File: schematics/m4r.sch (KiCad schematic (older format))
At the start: 93 parts

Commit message: Rename schematics folder and delete old board template
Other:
- note removed: "GLOBAL INTERCONNECTS"
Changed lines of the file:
@@
 Text Label 5550 9400 0    60   ~ 0
 JTCK
-Text Notes 650  750  0    98   ~ 20
-GLOBAL INTERCONNECTS
 $Comp
 L cusf-kicad:SWD_TC P?
@@
 JTDR
 Wire Notes Line
-	650  2950 3850 2950
-Wire Notes Line
-	3850 2950 3850 800
-Wire Notes Line
-	3850 800  650  800
-Wire Notes Line
-	650  800  650  2950
-Wire Notes Line
 	4400 8450 650  8450

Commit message: Chain JTAG connections
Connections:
- net JTDR renamed JTDO
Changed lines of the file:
@@
 JTDI
 Text Label 2950 4200 0    60   ~ 0
-JTDR
+JTDO
 Text Label 5550 9300 0    60   ~ 0
 JTMS
@@
 CAN_RXD
 Text Label 5550 9600 0    60   ~ 0
-JTDR
+JTDO
 Wire Notes Line
 	4400 8450 650  8450
@@
 JTDI
 Text HLabel 5400 9600 0    50   Input ~ 0
-JTDR
+JTDO
 Text HLabel 5400 9700 0    50   Input ~ 0
 3V3

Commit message: Master layout reorganisation and cleanup
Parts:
- removed C? (x2): 100n, agg:0402, symbol cusf-kicad:C
- removed C? (x2): 2µ2, agg:0402, symbol cusf-kicad:C
- removed D?: GRN, agg:0603-LED, symbol cusf-kicad:LED
- removed IC?: STM32F405RxTx, agg:LQFP-64, symbol cusf-kicad:STM32F405RxTx
- removed R?: 100, agg:0402, symbol cusf-kicad:R
- added C33, C38: 100n, agg:0402, symbol cusf-kicad:C
- added C42, C43: 2µ2, agg:0402, symbol cusf-kicad:C
- added D13: GRN, agg:0603-LED, symbol cusf-kicad:LED
- added IC9: STM32F405RxTx, agg:LQFP-64, symbol cusf-kicad:STM32F405RxTx
- added R16: 100, agg:0402, symbol cusf-kicad:R
- gave numbers to parts that had none: 86
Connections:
- net 3v3: now also C38.2, IC9.1 (VBAT), IC9.13 (VDDA), IC9.19 (VDD), IC9.32 (VDD), IC9.48 (VDD), IC9.64 (VDD)
- net 5V_CAN: now also C33.1
- net ANT_~EN: now also IC9.4 (PC15)
- net ANT_~FLAG: now also IC9.3 (PC14)
- net CAN_RXD: now also IC9.61 (PB8)
- net CAN_TXD: now also IC9.62 (PB9)
- net GND: now also C33.2, C38.1, C42.2, C43.2, D13.1, IC9.12 (VSSA), IC9.18 (VSS), IC9.60 (BOOT0), IC9.63 (VSS)
- net GPS_PPS: now also IC9.21 (PA5)
- net GPS_RESET_N: now also IC9.16 (PA2)
- net GPS_RX: now also IC9.14 (PA0)
- net GPS_TX: now also IC9.15 (PA1)
- net JTCK: now also IC9.49 (PA14)
- net JTDI: now also IC9.50 (PA15)
- net JTDO: now also IC9.55 (PB3)
- net JTMS: now also IC9.46 (PA13)
- net LED_GRN: now also IC9.11 (PC3), R16.1
- net LED_RED: now also IC9.9 (PC1)
- net LED_YLW: now also IC9.10 (PC2)
- net MCU_CLK: now also IC9.5 (PH0)
- net PLL_SCL: now also IC9.29 (PB10)
- net PLL_SDA: now also IC9.30 (PB11)
- net RADIO_GATE: now also IC9.41 (PA8)
- net RADIO_GPIO1: now also IC9.45 (PA12)
- net RADIO_SCLK: now also IC9.34 (PB13)
- net RADIO_SDI: now also IC9.36 (PB15)
- net RADIO_SDN: now also IC9.37 (PC6)
- net RADIO_SDO: now also IC9.35 (PB14)
- net RADIO_nIRQ: now also IC9.44 (PA11)
- net RADIO_nSEL: now also IC9.17 (PA3)
- net ~RST: now also IC9.7 (NRST)
- new net: D13.2, R16.2
- new net: C43.1, IC9.31 (VCAP_1)
- new net: C42.1, IC9.47 (VCAP_2)

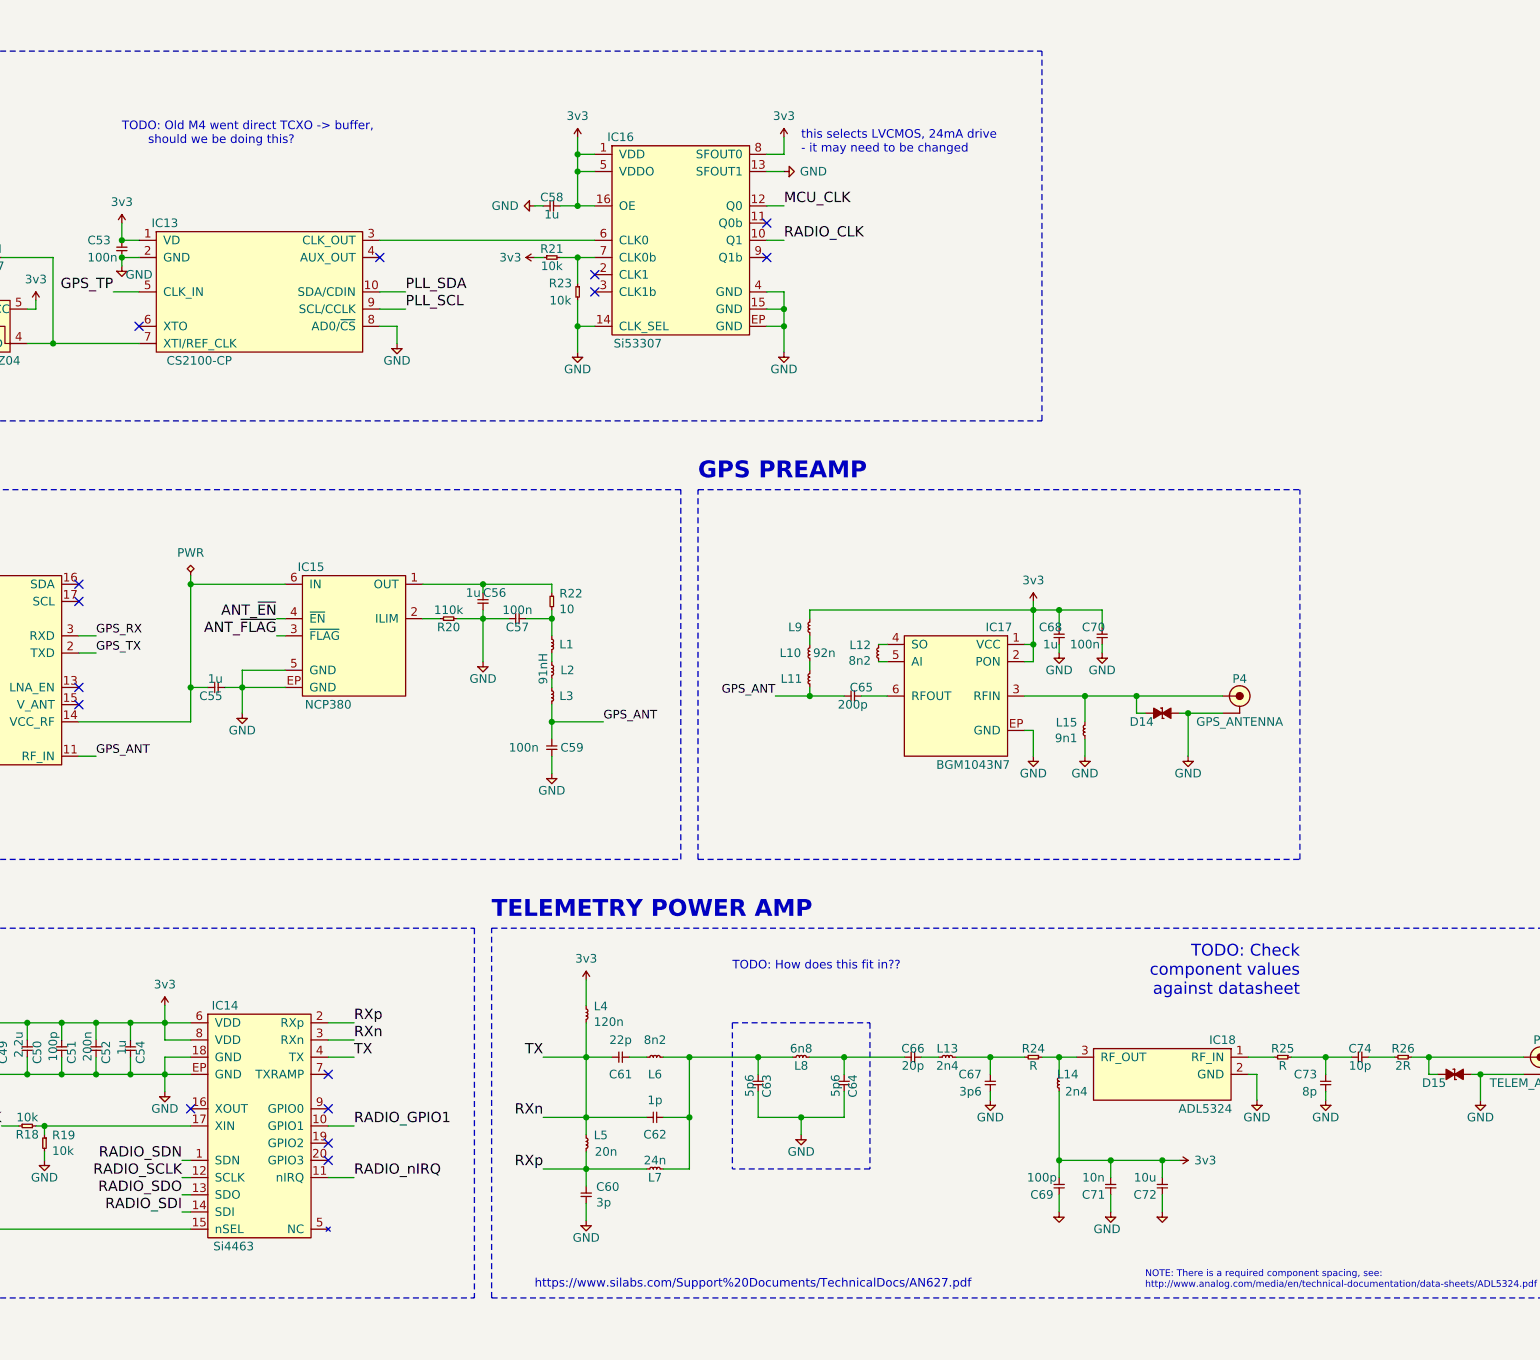
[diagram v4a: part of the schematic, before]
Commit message: Fix telemetry power amp
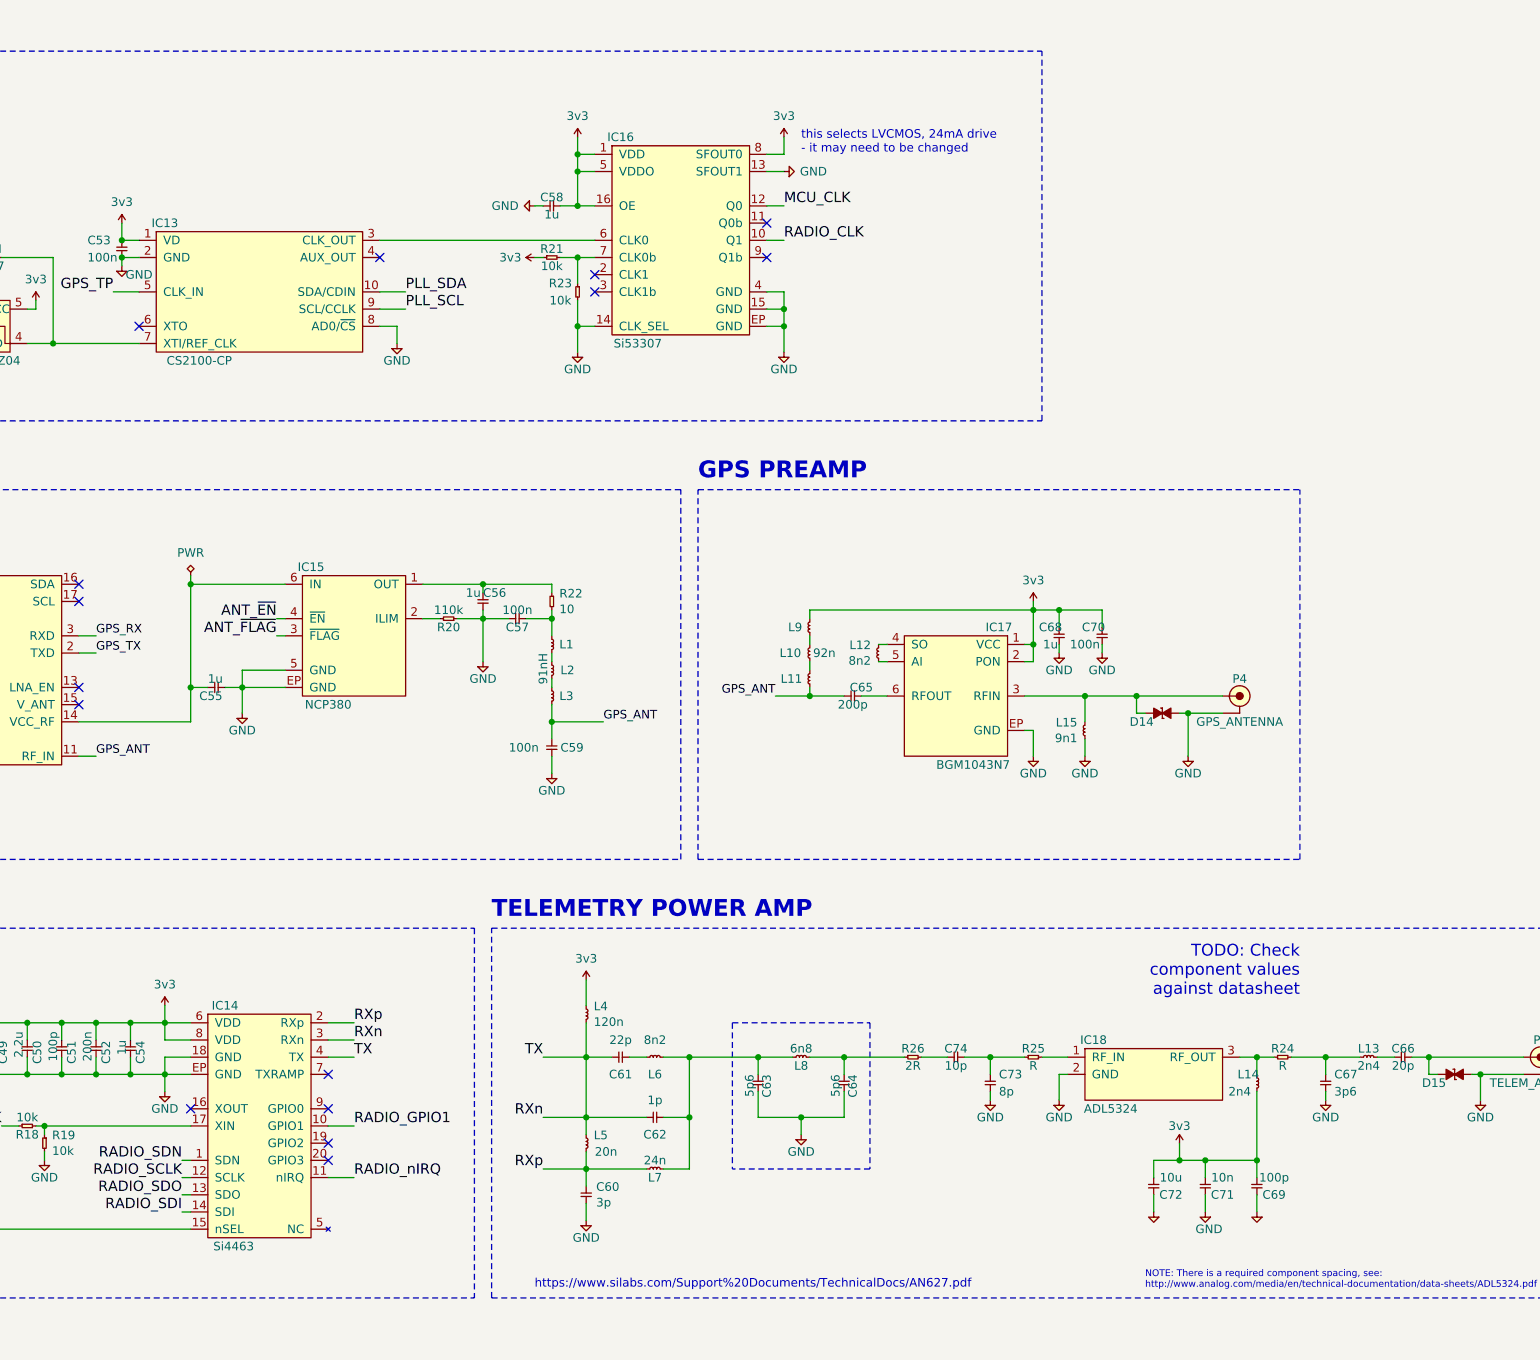
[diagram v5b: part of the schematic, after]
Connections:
- net at D15.2, P5.1 (RF): now also C66.2; no longer R26.1
- net at C64.1, L8.2: now also R26.1; no longer C66.2
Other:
- note removed: "TODO: How does this fit in??"
- note removed: "TODO: Old M4 went direct TCXO -> buffer,\n should we be doing this?"
- moved on the sheet: C66, C67, C69, C71, C72, C73, C74, IC18, L13, L14, R24, R25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

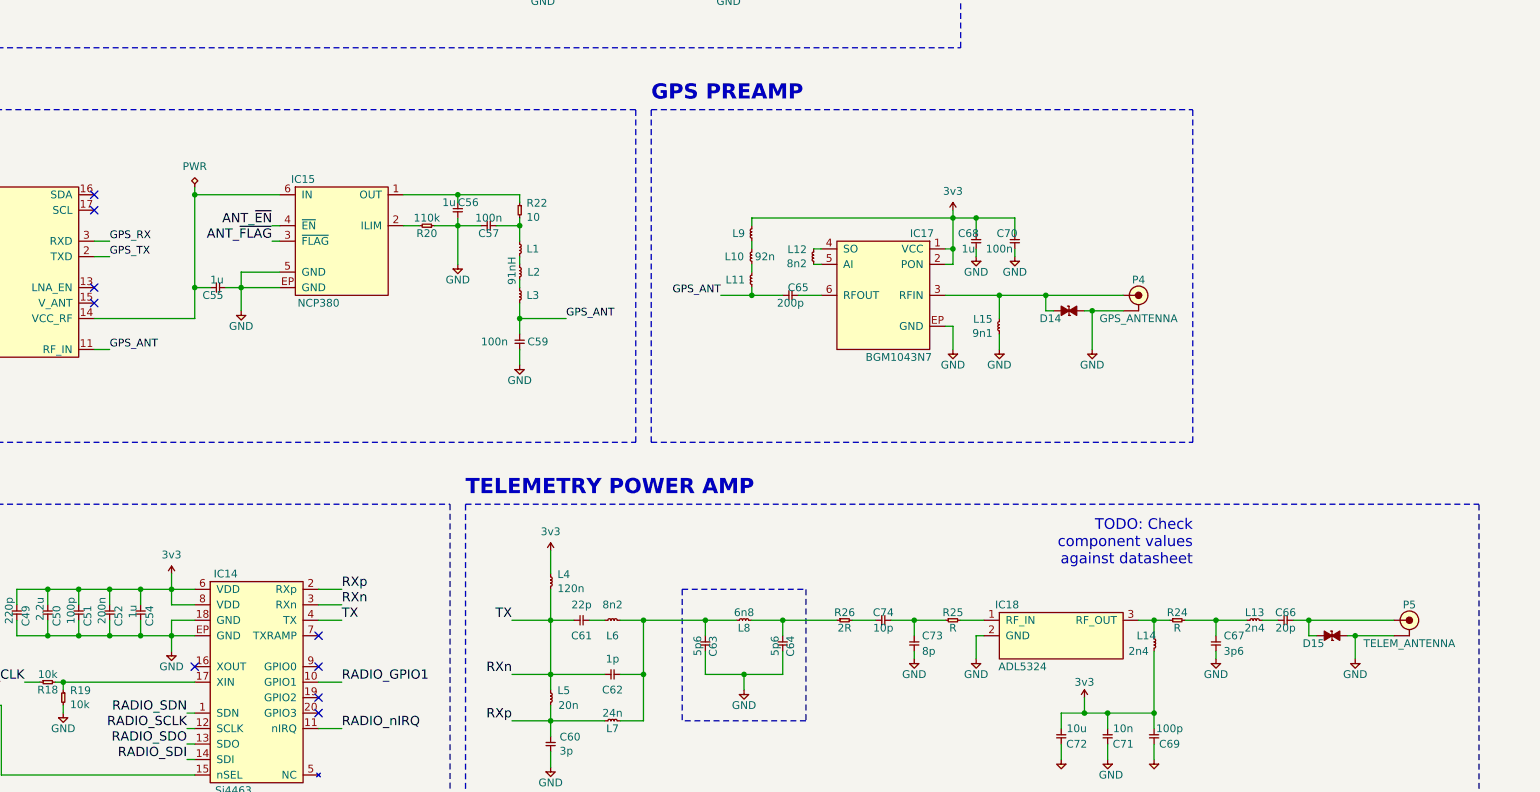
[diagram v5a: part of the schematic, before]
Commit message: Move master mcu to separate sheet
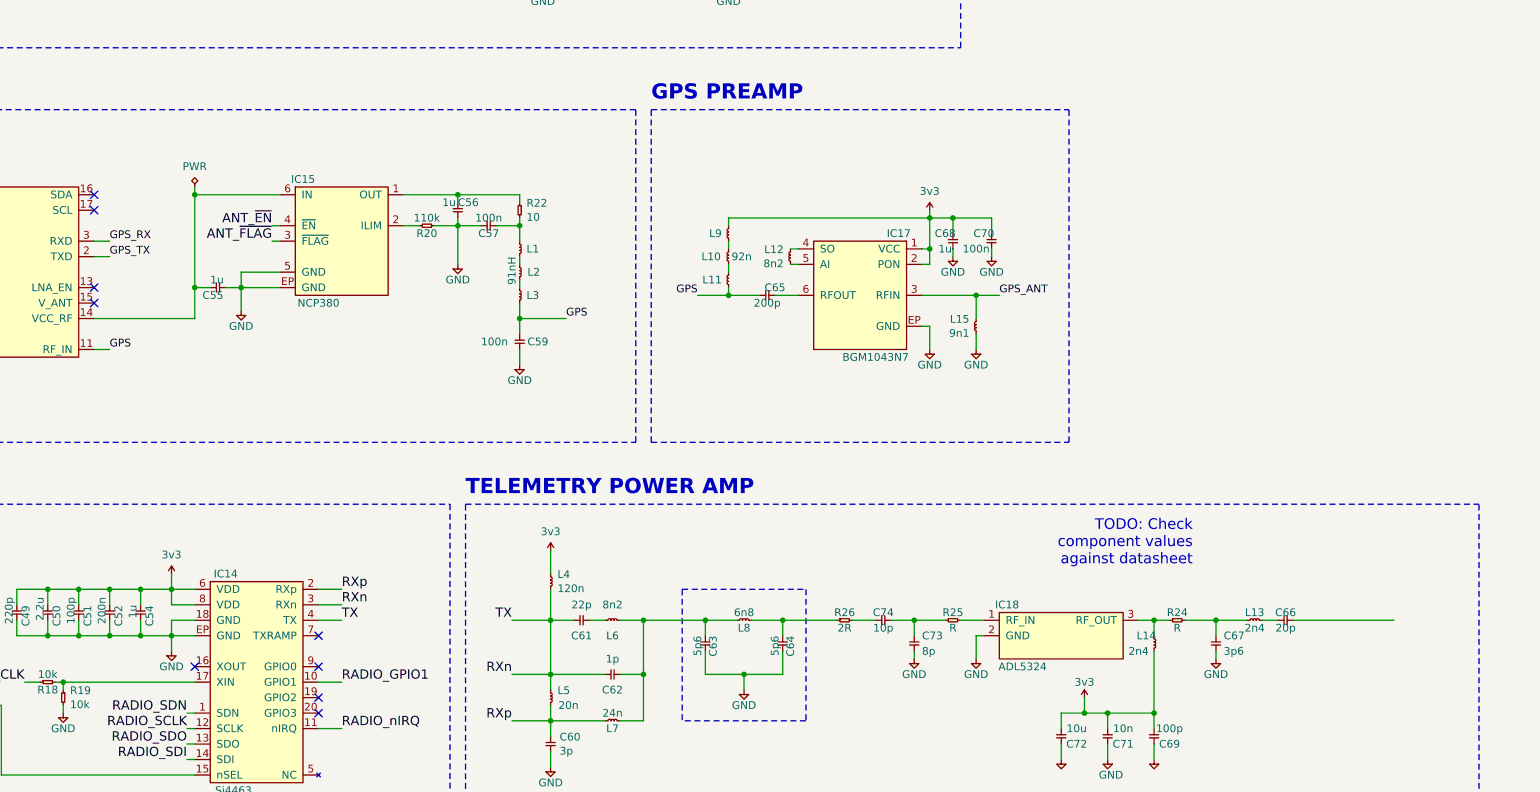
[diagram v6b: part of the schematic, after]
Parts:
- removed D14, D15: ESD_DIODE, agg:0402, symbol cusf-kicad:ESD_DIODE
- removed P4: GPS_ANTENNA, agg:SMA-EDGE, symbol cusf-kicad:COAX
- removed P5: TELEM_ANTENNA, agg:SMA-EDGE, symbol cusf-kicad:COAX
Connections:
- net GPS_ANT: now also IC17.3 (RFIN), L15.1; no longer C59.1, C65.2, IC11.11 (RF_IN), L11.2, L3.2
- new net GPS: C59.1, C65.2, IC11.11 (RF_IN), L11.2, L3.2
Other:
- moved on the sheet: C65, C68, C70, IC17, L10, L11, L12, L15, L9

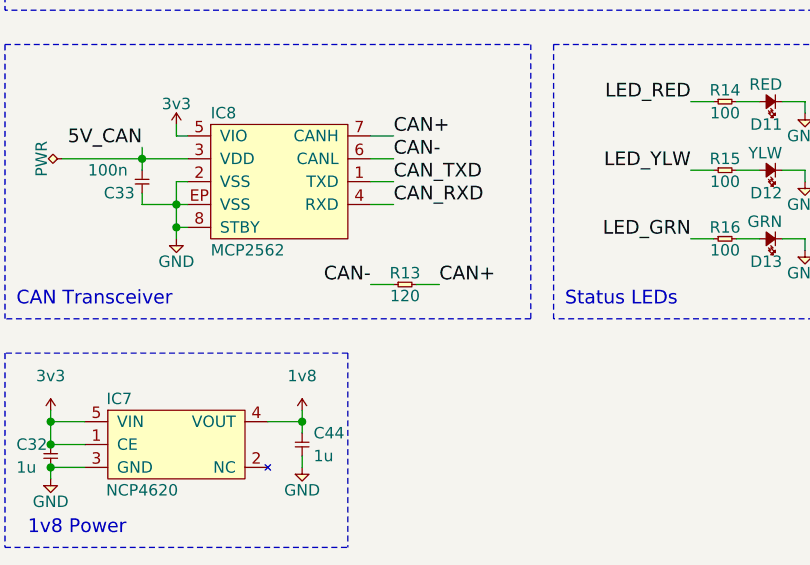
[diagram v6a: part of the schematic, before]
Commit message: Restructure main schematic bus layout
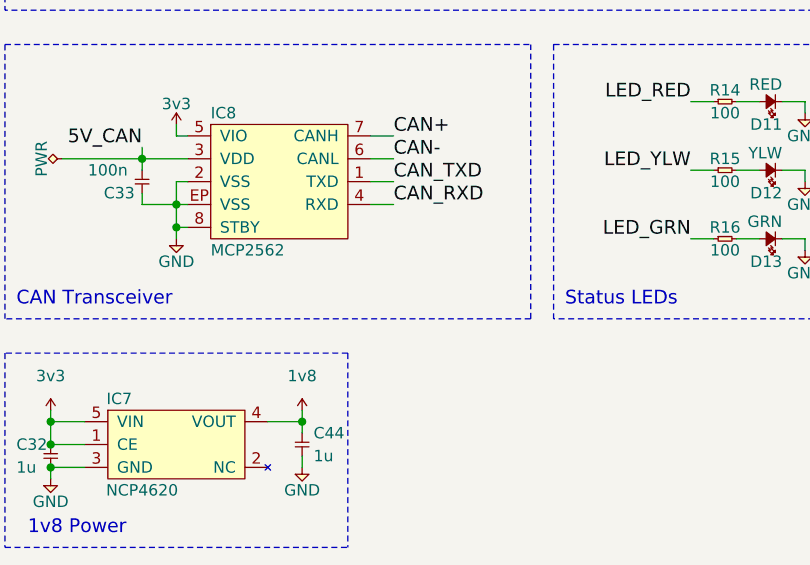
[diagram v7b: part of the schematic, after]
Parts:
- removed R13: 120, agg:0603, symbol cusf-kicad:R
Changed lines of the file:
@@
 	2850 5900 2950 5900
-$Comp
-L cusf-kicad:R R13
-U 1 1 5A9B48C6
-P 2350 9650
-F 0 "R13" H 2400 9700 50  0000 C CNN
-F 1 "120" H 2400 9600 50  0000 C CNN
-F 2 "agg:0603" H 2350 9650 50  0001 C CNN
-F 3 "" H 2350 9650 50  0001 C CNN
-F 4 "9238379" H 2350 9650 60  0001 C CNN "Farnell"
-	1    2350 9650
-	1    0    0    -1
-$EndComp
-Text Label 2250 9650 2    60   ~ 0
-CAN-
-Wire Wire Line
-	2250 9650 2350 9650
-Text Label 2550 9650 0    60   ~ 0
-CAN+
-Wire Wire Line
-	2550 9650 2450 9650
 $Comp
 L cusf-kicad:STM32F405RxTx IC9
